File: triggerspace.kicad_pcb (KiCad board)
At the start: 2 copper layers, 257.6 x 128.5 mm, 167 parts, among them J1 Conn_01x2, J10 Conn_01x12, J11 Conn_01x12, J12 Conn_02x05_Odd_Even, J13 Conn_01x10, J14 Conn_01x10, J15 Conn_01x10, J2 Conn_01x2, J3 Conn_01x4, J4 Conn_01x2, J4 Conn_01x4, J5 Conn_01x3, J6 Conn_01x3, J7 Conn_01x10, J8 Conn_01x3, Q1 2N3904, Q2 2N3904, U1 MCP6002_1, U2 MCP6002_1, U3 MCP6002_1, U4 L7805, U5 LM4040LP-5, U6 74HC595, U8 6N138, X1 CV_X, Y1 CV_Y

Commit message: Nano VIN from +12V, LED resistors, MIDI header labels/refdes, fix fab outputs
- A1 VIN (pin 30) moved from +5V to +12V, removing the v0.042 bodge. The +5V
  rail junction moves off pad 30 to a new via; VIN is routed on B.Cu to U4 IN.
- R25-R28 (LED resistors) 100r -> 4.7k, with "RL" silkscreen labels.
- Back-board 2-pin MIDI socket: was a PCB-only footprint duplicating the jack
  board's J4. Renamed J9 and added to the schematic on IN_MIDI/OUT_MIDI.
  Front D0/RX and D1/TX labels were swapped; corrected, and MIDI IN/OUT
  labels added on the back silkscreen.
- Regenerated back_pcb/jack_pcb fab outputs. The previous v0.5.0 outputs
  included the other board's tracks, vias and zones in each zip; the board
  split now removes those too. The back BOM no longer lists the jack's J4.
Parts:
- R25, R26, R27, R28: value 100r -> 4.7k
- renumbered J4 to J9
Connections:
- A1 pad 30: +5V -> +12V
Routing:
- net +12V: track 67.8 -> 112.2 mm
- net +5V: track 719.5 -> 718.7 mm, vias 2 -> 3
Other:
- board text added: "MIDI IN"
- board text added: "MIDI OUT"
- board text added: "RL"
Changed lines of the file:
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@@
 			(layers "*.Cu" "*.Mask")
 			(remove_unused_layers no)
-			(net 68 "+5V")
+			(net 40 "+12V")
 			(pinfunction "VIN")
 			(pintype "power_in")
@@
 			)
 		)
-		(property "Value" "100r"
+		(property "Value" "4.7k"
 			(at 3.81 2.37 90)
 			(layer "F.Fab")
@@
 			)
 		)
-		(property "Value" "100r"
+		(property "Value" "4.7k"
 			(at 3.81 2.37 90)
 			(layer "F.Fab")
@@
 			)
 		)
-		(property "Value" "100r"
+		(property "Value" "4.7k"
 			(at 3.81 2.37 90)
 			(layer "F.Fab")
@@
 			)
 		)
-		(property "Value" "100r"
+		(property "Value" "4.7k"
 			(at 3.81 2.37 90)
 			(layer "F.Fab")
@@
 		(descr "Through hole straight socket strip, 1x02, 2.54mm pitch, single row (from Kicad 4.0.7), script generated")
 		(tags "Through hole socket strip THT 1x02 2.54mm single row")
-		(property "Reference" "J4"
+		(property "Reference" "J9"
 			(at 0 2.77 0)
 			(layer "B.SilkS")
@@
 			)
 		)
-		(sheetfile "NanoGris.kicad_sch")
+		(sheetname "/")
+		(sheetfile "triggerspace.kicad_sch")
 		(attr through_hole)
 		(fp_line
@@
 		)
 	)
+	(gr_text "RL"
+		(at 123.6494 19.55 0)
+		(layer "F.SilkS")
+		(effects
+			(font
+				(size 1 1)
+				(thickness 0.15)
+			)
+		)
+	)
 	(gr_text "JLCJLCJLCJLC"
 		(locked yes)
@@
 		)
 	)
+	(gr_text "RL"
+		(at 126.8752 19.55 0)
+		(layer "F.SilkS")
+		(effects
+			(font
+				(size 1 1)
+				(thickness 0.15)
+			)
+		)
+	)
+	(gr_text "RL"
+		(at 130.1264 19.55 0)
+		(layer "F.SilkS")
+		(effects
+			(font
+				(size 1 1)
+				(thickness 0.15)
+			)
+		)
+	)
+	(gr_text "RL"
+		(at 133.276 19.55 0)
+		(layer "F.SilkS")
+		(effects
+			(font
+				(size 1 1)
+				(thickness 0.15)
+			)
+		)
+	)
 	(gr_text "JLCJLCJLCJLC"
 		(locked yes)
@@
 		)
 	)
-	(gr_text "D0/RX"
+	(gr_text "D1/TX"
 		(locked yes)
 		(at 112.465 24.265 0)
@@
 		)
 	)
-	(gr_text "D1/TX"
+	(gr_text "D0/RX"
 		(locked yes)
 		(at 112.465 26.709 0)
@@
 		)
 	)
+	(gr_text "MIDI IN"
+		(at 112.690475 26.702626 0)
+		(layer "B.SilkS")
+		(effects
+			(font
+				(size 1 1)
+				(thickness 0.2)
+			)
+			(justify mirror)
+		)
+	)
+	(gr_text "MIDI OUT"
+		(at 113.357142 24.162626 0)
+		(layer "B.SilkS")
+		(effects
+			(font
+				(size 1 1)
+				(thickness 0.2)
+			)
+			(justify mirror)
+		)
+	)
 	(gr_text "{dblquote}triggerspace{dblquote}"
 		(locked yes)
@@
 	)
 	(segment
+		(start 166.878 59.436)
+		(end 166.878 78.994)
+		(width 0.25)
+		(layer "B.Cu")
+		(net 40)
+	)
+	(segment
 		(start 156.591 111.379)
 		(end 156.591 92.688114)
@@
 	)
 	(segment
+		(start 155.702 48.26)
+		(end 166.878 59.436)
+		(width 0.25)
+		(layer "B.Cu")
+		(net 40)
+	)
+	(segment
+		(start 148.59 48.26)
+		(end 155.702 48.26)
+		(width 0.25)
+		(layer "B.Cu")
+		(net 40)
+	)
+	(segment
 		(start 153.67 113.03)
 		(end 154.94 113.03)
@@
 	)
 	(segment
+		(start 166.37 79.502)
+		(end 165.712493 80.454426)
+		(width 0.25)
+		(layer "B.Cu")
+		(net 40)
+	)
+	(segment
 		(start 154.94 113.03)
 		(end 156.591 111.379)
@@
 	)
 	(segment
+		(start 166.878 78.994)
+		(end 166.37 79.502)
+		(width 0.25)
+		(layer "B.Cu")
+		(net 40)
+	)
+	(segment
 		(start 137.013624 92.563624)
 		(end 135.850047 92.563624)
@@
 	)
 	(segment
+		(start 149.86 44.96)
+		(end 151.22 46.32)
+		(width 0.25)
+		(layer "F.Cu")
+		(net 68)
+	)
+	(segment
 		(start 161.404 40.629)
 		(end 158.782 40.629)
@@
 	)
 	(segment
-		(start 147.1168 44.958)
-		(end 148.59 46.4312)
+		(start 242.37 30.48)
+		(end 244.29 32.4)
 		(width 0.25)
 		(locked yes)
@@
 	)
 	(segment
-		(start 242.37 30.48)
-		(end 244.29 32.4)
+		(start 120.65 73.66)
+		(end 122.390001 75.400001)
 		(width 0.25)
 		(locked yes)
@@
 	)
 	(segment
-		(start 120.65 73.66)
-		(end 122.390001 75.400001)
+		(start 151.22 48.26)
+		(end 151.22 50.68)
 		(width 0.25)
-		(locked yes)
 		(layer "F.Cu")
 		(net 68)
@@
 	)
 	(segment
-		(start 148.642009 48.312009)
-		(end 148.59 48.26)
-		(width 0.25)
-		(locked yes)
-		(layer "F.Cu")
-		(net 68)
-	)
-	(segment
 		(start 139.650859 55.92)
 		(end 142.333767 53.237092)
@@
 	)
 	(segment
+		(start 151.22 50.68)
+		(end 148.64 50.68)
+		(width 0.25)
+		(layer "F.Cu")
+		(net 68)
+	)
+	(segment
 		(start 163.059 38.974)
 		(end 161.404 40.629)
@@
 	)
 	(segment
+		(start 147.12 44.96)
+		(end 149.86 44.96)
+		(width 0.25)
+		(layer "F.Cu")
+		(net 68)
+	)
+	(segment
 		(start 210.41 33.02)
 		(end 212.95 30.48)
@@
 	)
 	(segment
+		(start 151.22 46.32)
+		(end 151.22 48.26)
+		(width 0.25)
+		(layer "F.Cu")
+		(net 68)
+	)
+	(segment
 		(start 247.307916 32.9)
 		(end 256.267916 41.86)
@@
 	)
 	(segment
-		(start 148.59 46.4312)
-		(end 148.59 48.26)
-		(width 0.25)
-		(locked yes)
-		(layer "F.Cu")
-		(net 68)
-	)
-	(segment
 		(start 217.149053 90.0176)
 		(end 219.284719 92.153266)
@@
 	)
 	(segment
-		(start 150.99 48.26)
-		(end 148.59 48.26)
-		(width 0.25)
-		(locked yes)
-		(layer "F.Cu")
-		(net 68)
-	)
-	(segment
 		(start 199.39 54.9148)
 		(end 201.6252 57.15)
@@
 	)
 	(segment
-		(start 148.642009 50.681576)
-		(end 148.642009 48.312009)
-		(width 0.25)
-		(locked yes)
-		(layer "F.Cu")
-		(net 68)
-	)
-	(segment
 		(start 260.060453 85.837988)
 		(end 260.060453 82.799253)
@@
 	)
 	(segment
-		(start 151.219 48.26)
-		(end 150.99 48.26)
-		(width 0.25)
-		(layer "F.Cu")
-		(net 68)
-	)
-	(segment
 		(start 142.333767 53.237092)
 		(end 146.086493 53.237092)
@@
 	)
 	(via
+		(at 151.22 50.68)
+		(size 0.8)
+		(drill 0.4)
+		(layers "F.Cu" "B.Cu")
+		(net 68)
+	)
+	(via
 		(at 217.149053 90.0176)
 		(size 0.8)
@@
 	)
 	(segment
-		(start 148.59 53.34)
-		(end 151.13 55.88)
-		(width 0.25)
-		(locked yes)
-		(layer "B.Cu")
-		(net 68)
-	)
-	(segment
 		(start 127 76.2)
 		(end 123.19 76.2)
@@
 	)
 	(segment
+		(start 151.22 55.79)
+		(end 151.22 50.68)
+		(width 0.25)
+		(layer "B.Cu")
+		(net 68)
+	)
+	(segment
 		(start 259.060453 49.710453)
 		(end 259.060453 53.38)
@@
 	)
 	(segment
-		(start 148.59 48.26)
-		(end 148.59 53.34)
-		(width 0.25)
-		(locked yes)
-		(layer "B.Cu")
-		(net 68)
-	)
-	(segment
 		(start 198.214999 119.474999)
 		(end 198.214999 94.859999)
@@
 		(layer "B.Cu")
 		(net 68)
+	)
+	(segment
+		(start 151.13 55.88)
+		(end 151.22 55.79)
+		(width 0.25)
+		(layer "B.Cu")
+		(net 68)

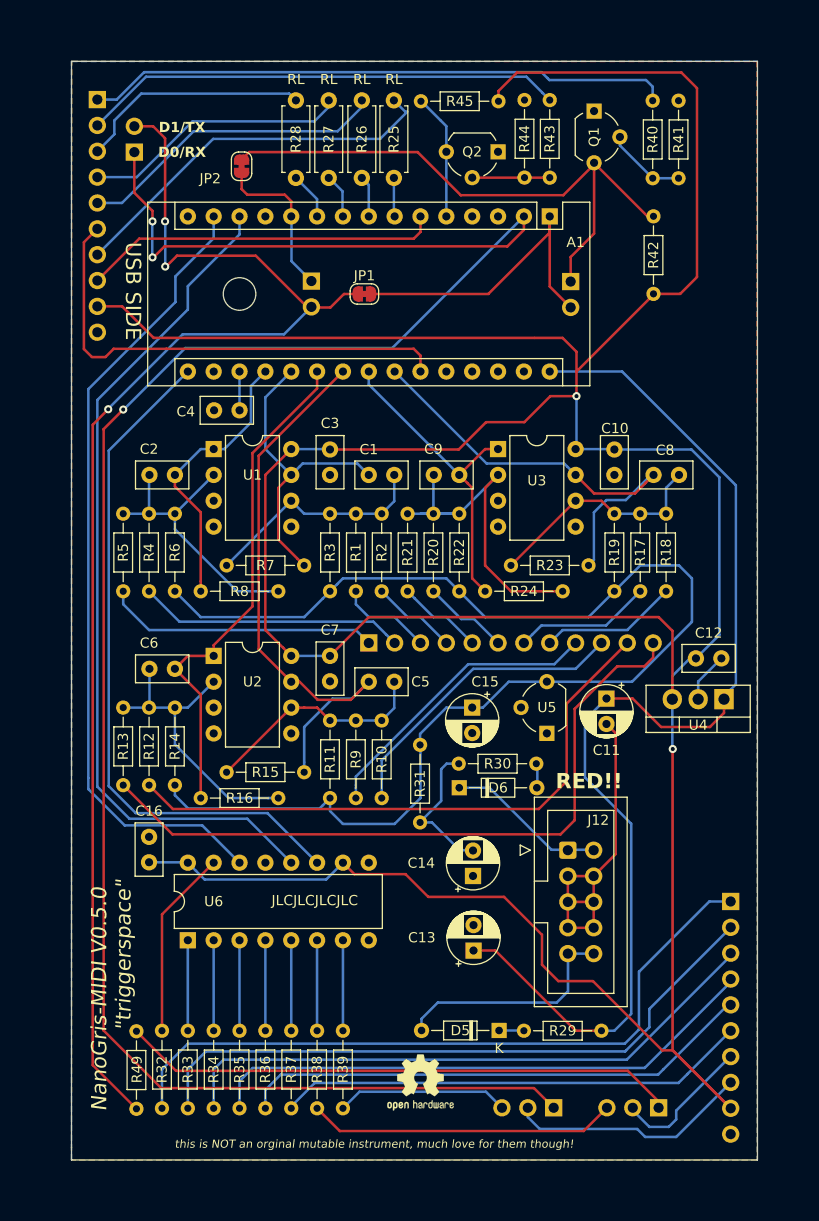
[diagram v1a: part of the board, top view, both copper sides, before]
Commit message: U4 lies flat (TO-220 tab-down), back PCB outline shifted 1mm
- U4 (L7805) swapped to TO-220-3_Horizontal_TabDown, pin 1 at (165.0, 78.5),
  body lying over the free area above J7. Only the GND pour is on F.Cu under
  the tab (with GND stitching vias); +5V/+12V rerouted on B.Cu or between the
  pin row and the body. C12 moved up 0.94mm to make room.
- Back PCB outline (and its zones) moved 1mm (-x in the file, right as seen
  from the front panel). Parts and inter-board headers are unchanged; checked
  against all 33 mating header/standoff pins that the left edge is now flush
  with the jack PCB to within 0.09mm.
- Regenerated back_pcb/jack_pcb fab outputs.
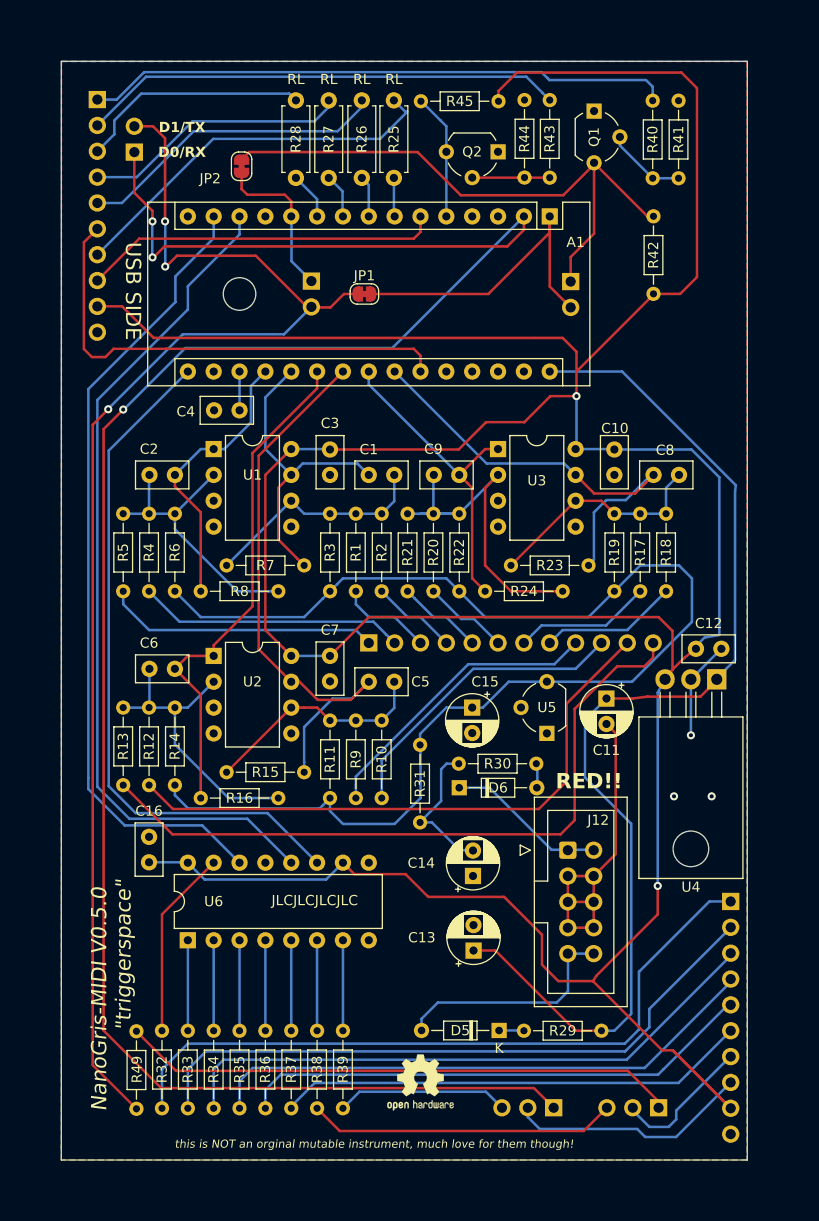
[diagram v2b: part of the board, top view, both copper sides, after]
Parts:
- U4: footprint Package_TO_SOT_THT:TO-220-3_Vertical -> Package_TO_SOT_THT:TO-220-3_Horizontal_TabDown
- moved U4 2.08 mm to (165.0, 78.5)
- moved C12 0.94 mm to (163.0, 75.5)
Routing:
- net +5V: track 718.7 -> 712.3 mm
- net GND: track 134.6 -> 139.4 mm, vias 0 -> 3
- net +12V: track 112.2 -> 107.5 mm
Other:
- outline, holes or cut-outs redrawn

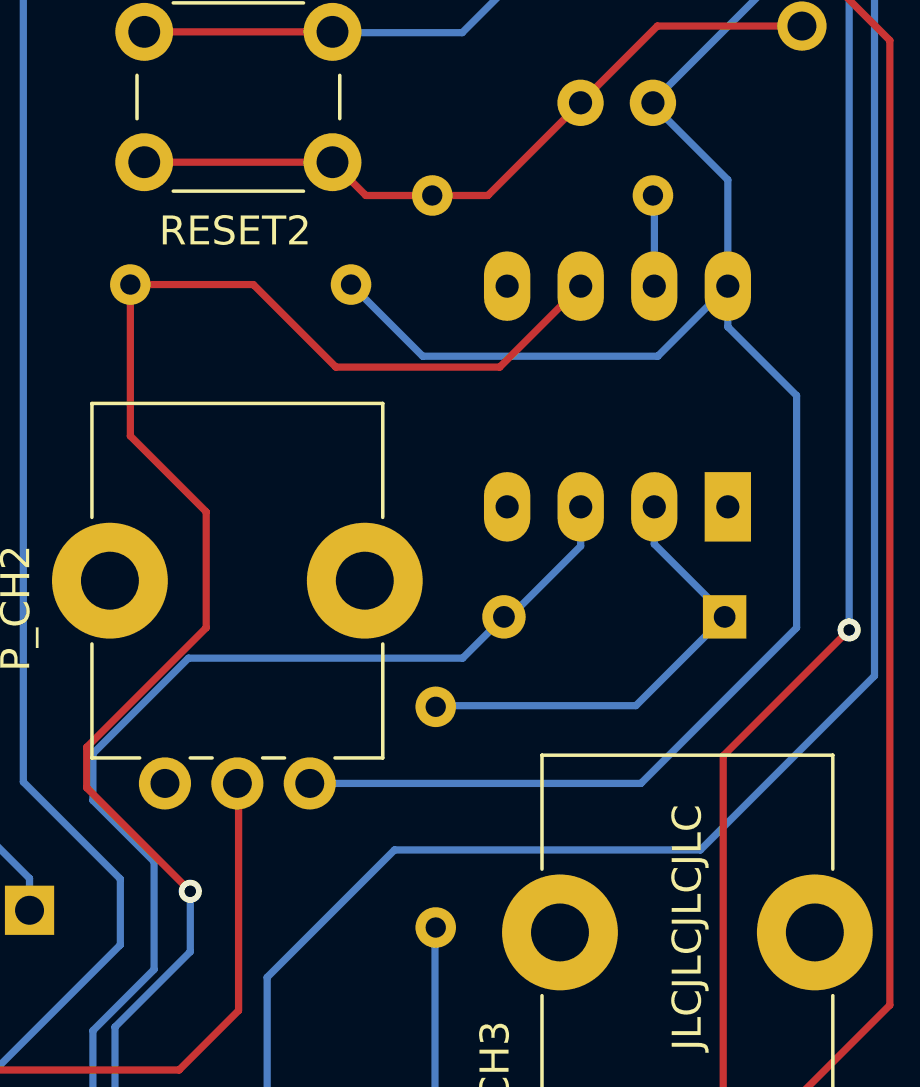
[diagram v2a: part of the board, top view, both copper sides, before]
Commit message: LPZW auto-crossover MIDI IN (TRS Type A/B) with SOIC-8 and 6N138 build options
U8 becomes an HCPL-2630 dual optocoupler wired as the LPZW auto-crossover
MIDI input (Kay Knofe / LPZW.modules, credited on the jack PCB silkscreen):
two anti-parallel LEDs across tip and ring with their own 220R (R48, new
R51), wire-ORed open-collector outputs, pull-up R47 220R -> 1k.

- U9: optional HCPL-0630 SOIC-8 footprint inside U8's DIP-8 footprint
- JP3/JP4 3-pad solder jumpers (1-2 bridged) and optional D7 keep a
  6N138 build possible (cut 1-2, bridge 2-3, fit D7)
- R46 to 5.08mm pitch; D7 moved and DNP; local re-place/re-route around U8
- README: Build options section; CHANGELOG v0.5.0 entries
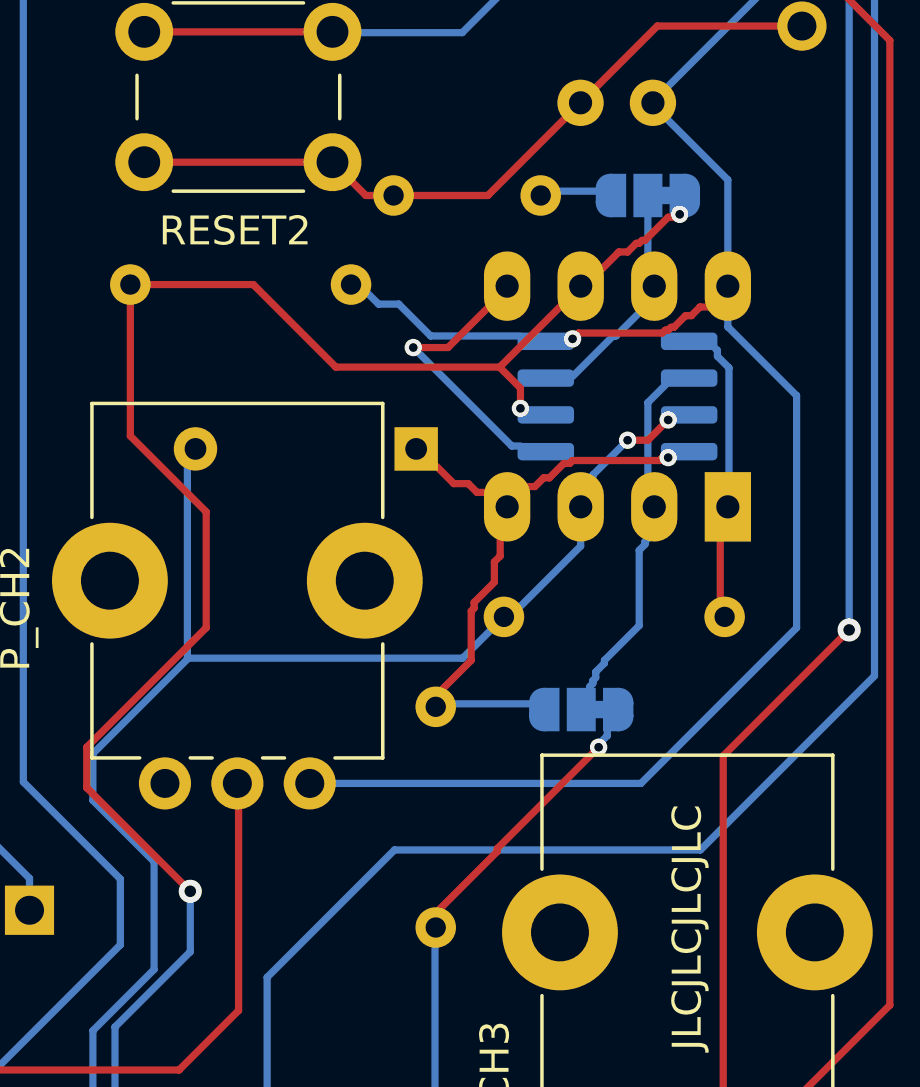
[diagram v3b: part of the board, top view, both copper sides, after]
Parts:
- added JP3: SolderJumper_3_Bridged12, Jumper:SolderJumper-3_P1.3mm_Bridged12_RoundedPad1.0x1.5mm_NumberLabels, B.Cu at (254.0, 68.0)
- added JP4: SolderJumper_3_Bridged12, Jumper:SolderJumper-3_P1.3mm_Bridged12_RoundedPad1.0x1.5mm_NumberLabels, B.Cu at (256.3, 50.2)
- added R51: 220, Resistor_THT:R_Axial_DIN0204_L3.6mm_D1.6mm_P7.62mm_Horizontal, B.Cu at (251.3, 64.8)
- added U9: HCPL-0630, Package_SO:SOIC-8_3.9x4.9mm_P1.27mm, B.Cu at (255.2, 57.2)
- R46: footprint Resistor_THT:R_Axial_DIN0204_L3.6mm_D1.6mm_P7.62mm_Horizontal -> Resistor_THT:R_Axial_DIN0204_L3.6mm_D1.6mm_P5.08mm_Horizontal
- R47: value 220 -> 1k
- U8: value 6N138 -> HCPL-2630
- moved D7 12.1 mm to (248.3, 59.0)
- moved R46 3.88 mm to (252.6, 50.2)
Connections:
- net Net-(D7-A) renamed /MIDI_TIP
- net Net-(J4-Pin_4) renamed /MIDI_RING
- net Net-(J8-Pin_3) renamed /OPTO_OUT
- D7 pad 1: Net-(D7-K) -> /OPTO_A2
- R46 pad 1: Net-(U8-VO1) -> Net-(JP4-B)
- R48 pad 2: Net-(D7-K) -> /OPTO_A2
- U8 pad 1: unconnected-(U8-NC-Pad1) -> /OPTO_A1
- U8 pad 2: Net-(D7-K) -> /OPTO_C1
- U8 pad 4: unconnected-(U8-NC-Pad4) -> /OPTO_A2
- U8 pad 7: Net-(U8-VO1) -> /OPTO_VO1
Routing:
- net /OPTO_A2: track 0.00 -> 16.1 mm, vias 0 -> 1
- net Net-(D7-K): track 16.1 -> 0.00 mm
- net /MIDI_TIP: track 102.4 -> 112.5 mm, vias 0 -> 2
- net /OPTO_C1: track 0.00 -> 9.48 mm
- net /MIDI_RING: track 45.5 -> 54.2 mm, vias 0 -> 1
- net GND: track 139.4 -> 147.7 mm, vias 3 -> 4
- net /OPTO_A1: track 0.00 -> 6.71 mm
- net /OPTO_OUT: track 91.5 -> 96.6 mm, vias 1 -> 3
- net /OPTO_VO1: track 0.00 -> 4.61 mm
- net +5V: track 712.3 -> 708.4 mm, vias 3 -> 4
- net Net-(U8-VO1): track 3.15 -> 0.00 mm
- net Net-(JP4-B): track 0.00 -> 1.40 mm
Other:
- board text added: "AUTO-CROSSOVER"
- board text added: "MIDI IN: LPZW"
